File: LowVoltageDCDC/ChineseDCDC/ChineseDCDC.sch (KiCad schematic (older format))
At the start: 22 parts, among them J1 Conn_01x02, J2 Conn_01x02, J3 Conn_01x02, J4 Conn_01x02, J5 Conn_01x03, J6 Conn_01x02, J7 Conn_01x02, U1 MP3414, U2 SC6206B - SHEN ZHEN, U3 LN1134 - NATLINEAR

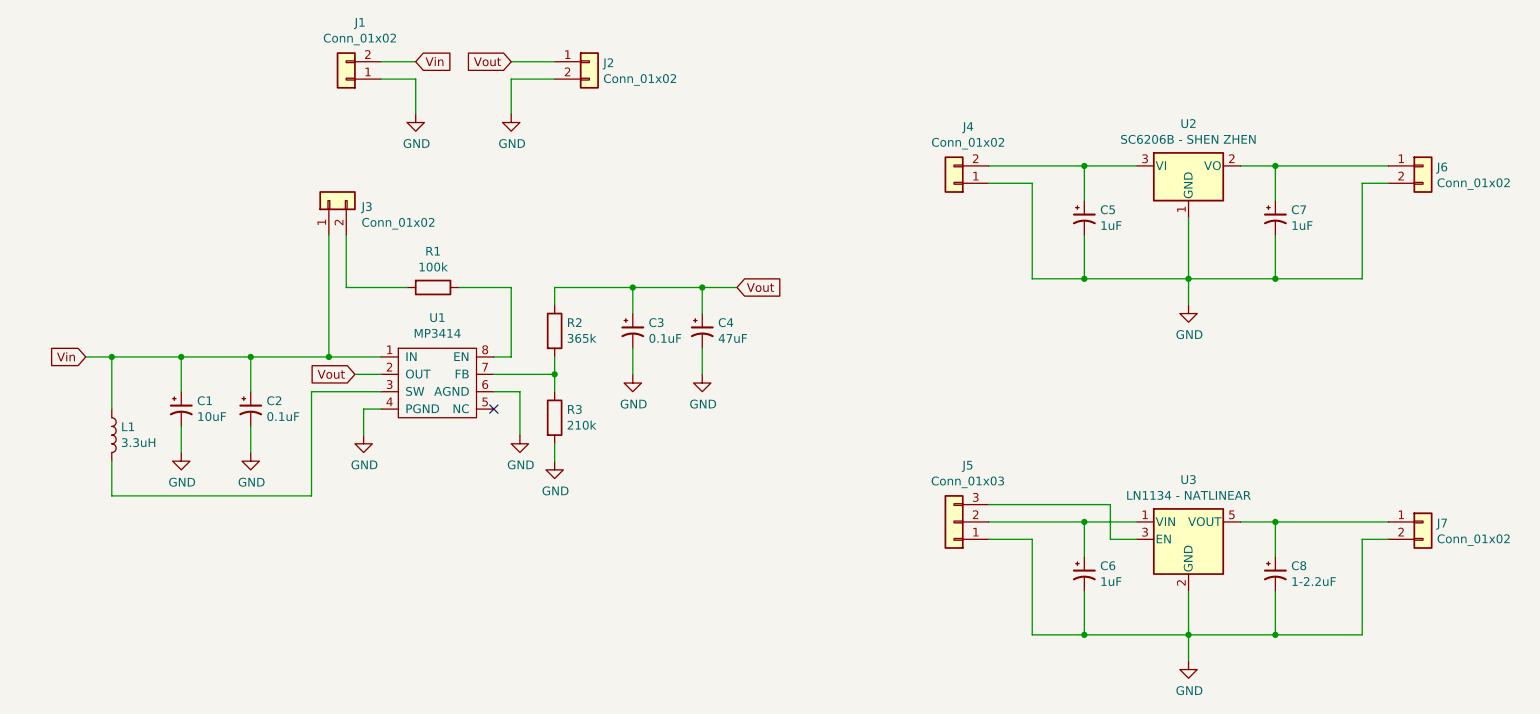
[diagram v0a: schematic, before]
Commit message: modificando disposição no esquemático, mas não o esquemático em si
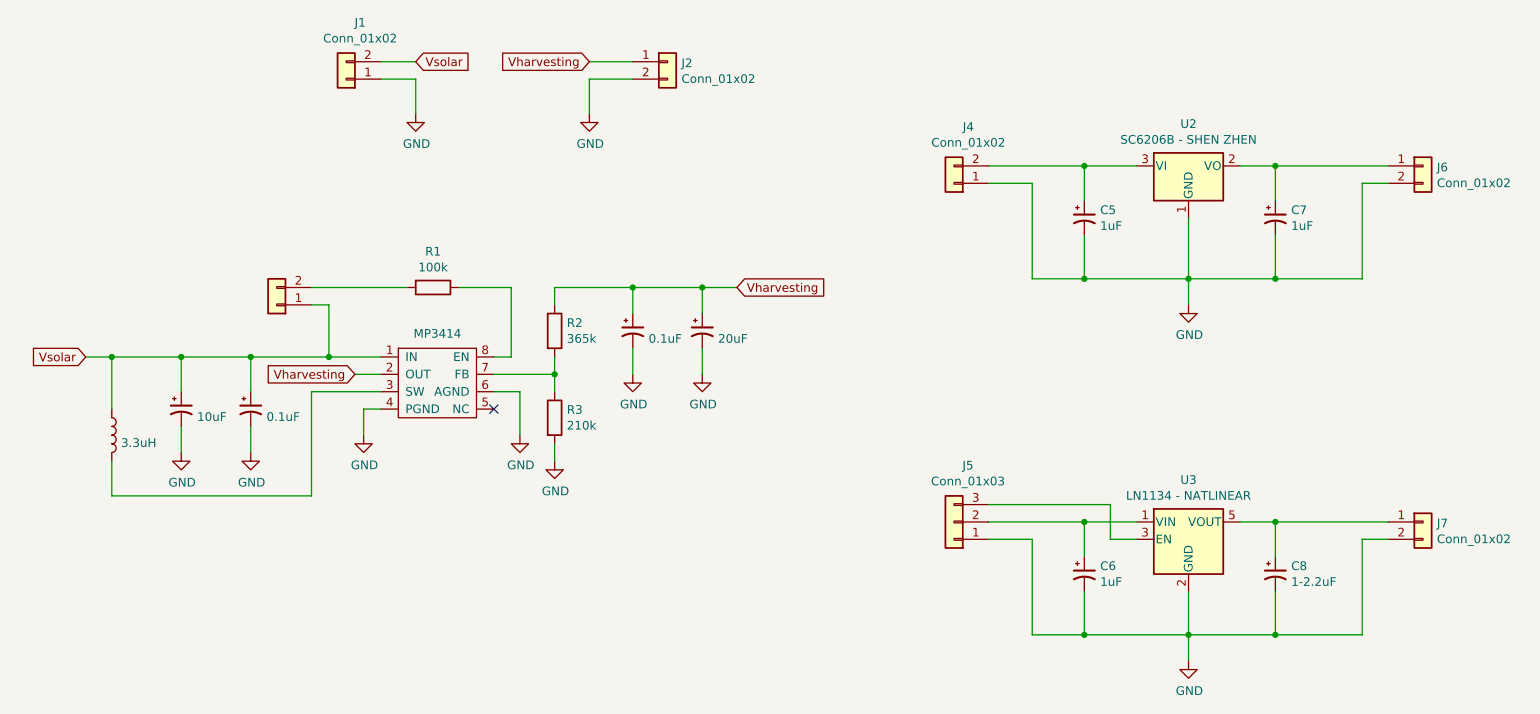
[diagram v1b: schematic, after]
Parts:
- C4: value 47uF -> 20uF
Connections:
- net Vin renamed Vsolar
- net Vout renamed Vharvesting
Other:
- moved on the sheet: J2
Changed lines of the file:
@@
 U 1 1 5C051F52
 P 1750 3500
-F 0 "L1" H 1803 3546 50  0000 L CNN
+F 0 "L1" H 1803 3546 50  0001 L CNN
 F 1 "3.3uH" H 1803 3455 50  0000 L CNN
 F 2 "Inductors_SMD:L_Taiyo-Yuden_NR-60xx_HandSoldering" H 1750 3500 50  0001 C CNN
@@
 U 1 1 5C0520BE
 P 2150 3350
-F 0 "C1" H 2241 3396 50  0000 L CNN
+F 0 "C1" H 2241 3396 50  0001 L CNN
 F 1 "10uF" H 2241 3305 50  0000 L CNN
 F 2 "Capacitors_SMD:C_1206_HandSoldering" H 2150 3350 50  0001 C CNN
@@
 U 1 1 5C05224E
 P 2550 3350
-F 0 "C2" H 2641 3396 50  0000 L CNN
+F 0 "C2" H 2641 3396 50  0001 L CNN
 F 1 "0.1uF" H 2641 3305 50  0000 L CNN
 F 2 "Capacitors_SMD:C_0805_HandSoldering" H 2550 3350 50  0001 C CNN
@@
 	4050 3050 3950 3050
 Text GLabel 3150 3150 0    50   Input ~ 0
-Vout
+Vharvesting
 Wire Wire Line
 	3150 3150 3300 3150
 Text GLabel 5350 2650 2    50   Input ~ 0
-Vout
+Vharvesting
 $Comp
 L Device:R R2
@@
 L Connector_Generic:Conn_01x02 J2
 U 1 1 5C0542A2
-P 4500 1350
-F 0 "J2" H 4580 1342 50  0000 L CNN
-F 1 "Conn_01x02" H 4580 1251 50  0000 L CNN
-F 2 "TerminalBlock:TerminalBlock_Altech_AK300-2_P5.00mm" H 4500 1350 50  0001 C CNN
-F 3 "~" H 4500 1350 50  0001 C CNN
-	1    4500 1350
-	1    0    0    -1
-$EndComp
-Text GLabel 4050 1350 0    50   Input ~ 0
-Vout
-Wire Wire Line
-	4050 1350 4300 1350
+P 4950 1350
+F 0 "J2" H 5030 1342 50  0000 L CNN
+F 1 "Conn_01x02" H 5030 1251 50  0000 L CNN
+F 2 "TerminalBlock:TerminalBlock_Altech_AK300-2_P5.00mm" H 4950 1350 50  0001 C CNN
+F 3 "~" H 4950 1350 50  0001 C CNN
+	1    4950 1350
+	1    0    0    -1
+$EndComp
+Text GLabel 4500 1350 0    50   Input ~ 0
+Vharvesting
+Wire Wire Line
+	4500 1350 4750 1350
 $Comp
 L ChineseDCDC-rescue:GND-power #PWR0107
 U 1 1 5C054747
-P 4050 1650
-F 0 "#PWR0107" H 4050 1400 50  0001 C CNN
-F 1 "GND" H 4055 1477 50  0000 C CNN
-F 2 "" H 4050 1650 50  0001 C CNN
-F 3 "" H 4050 1650 50  0001 C CNN
-	1    4050 1650
-	1    0    0    -1
-$EndComp
-Wire Wire Line
-	4050 1650 4050 1450
-Wire Wire Line
-	4050 1450 4300 1450
+P 4500 1650
+F 0 "#PWR0107" H 4500 1400 50  0001 C CNN
+F 1 "GND" H 4505 1477 50  0000 C CNN
+F 2 "" H 4500 1650 50  0001 C CNN
+F 3 "" H 4500 1650 50  0001 C CNN
+	1    4500 1650
+	1    0    0    -1
+$EndComp
+Wire Wire Line
+	4500 1650 4500 1450
+Wire Wire Line
+	4500 1450 4750 1450
 NoConn ~ 3950 3350
 Text GLabel 3500 1350 2    50   Input ~ 0
-Vin
+Vsolar
 Wire Wire Line
 	3500 1350 3300 1350
 Text GLabel 1600 3050 0    50   Input ~ 0
-Vin
+Vsolar
 Wire Wire Line
 	1600 3050 1750 3050
@@
 U 1 1 5C059925
 P 5150 2900
-F 0 "C4" H 5241 2946 50  0000 L CNN
-F 1 "47uF" H 5241 2855 50  0000 L CNN
+F 0 "C4" H 5241 2946 50  0001 L CNN
+F 1 "20uF" H 5241 2855 50  0000 L CNN
 F 2 "Capacitors_SMD:C_1206_HandSoldering" H 5150 2900 50  0001 C CNN
 F 3 "" H 5150 2900 50  0001 C CNN
@@
 U 1 1 5C059A03
 P 4750 2900
-F 0 "C3" H 4841 2946 50  0000 L CNN
+F 0 "C3" H 4841 2946 50  0001 L CNN
 F 1 "0.1uF" H 4841 2855 50  0000 L CNN
 F 2 "Capacitors_SMD:C_0805_HandSoldering" H 4750 2900 50  0001 C CNN
@@
 U 1 1 5C058492
 P 3600 3200
-F 0 "U1" H 3625 3575 50  0000 C CNN
+F 0 "U1" H 3625 3575 50  0001 C CNN
 F 1 "MP3414" H 3625 3484 50  0000 C CNN
 F 2 "TO_SOT_Packages_SMD:SOT-23-8_Handsoldering" H 3700 2850 50  0001 C CNN
@@
 	1    0    0    -1
 $EndComp
-Wire Wire Line
-	2550 3050 3000 3050
-Wire Wire Line
-	3100 2650 3100 2350
-Wire Wire Line
-	3100 2650 3450 2650
 $Comp
 L Connector_Generic:Conn_01x02 J3
 U 1 1 5C0DAE06
-P 3000 2150
-F 0 "J3" V 2964 1962 50  0000 R CNN
-F 1 "Conn_01x02" V 2873 1962 50  0000 R CNN
-F 2 "Pin_Headers:Pin_Header_Straight_1x02_Pitch2.54mm" H 3000 2150 50  0001 C CNN
-F 3 "~" H 3000 2150 50  0001 C CNN
-	1    3000 2150
-	0    -1   -1   0
-$EndComp
-Wire Wire Line
-	3000 2350 3000 3050
-Connection ~ 3000 3050
-Wire Wire Line
-	3000 3050 3300 3050
+P 2700 2750
+F 0 "J3" H 2750 2550 50  0001 R CNN
+F 1 "Conn_01x02" H 2750 2450 50  0001 R CNN
+F 2 "Pin_Headers:Pin_Header_Straight_1x02_Pitch2.54mm" H 2700 2750 50  0001 C CNN
+F 3 "~" H 2700 2750 50  0001 C CNN
+	1    2700 2750
+	-1   0    0    1
+$EndComp
 $Comp
 L Connector_Generic:Conn_01x02 J4
@@
 Wire Wire Line
 	7500 3900 6800 3900
+Wire Wire Line
+	2550 3050 3000 3050
+Wire Wire Line
+	2900 2750 3000 2750
+Wire Wire Line
+	3000 2750 3000 3050
+Connection ~ 3000 3050
+Wire Wire Line
+	3000 3050 3300 3050
+Wire Wire Line
+	2900 2650 3450 2650
 $EndSCHEMATC
